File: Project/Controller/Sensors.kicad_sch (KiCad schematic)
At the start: 8 parts, among them J4 Conn_01x04, U3 BMI088, U4 MMC5983MA

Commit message: Add LDO to power input for controller board
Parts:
- renumbered C17 to C18, C18 to C19, C19 to C20, C20 to C21, C21 to C22, U3 to U5, U4 to U6
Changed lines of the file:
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@@
 		(dnp no)
 		(fields_autoplaced yes)
-		(property "Reference" "#PWR037"
+		(property "Reference" "#PWR040"
 			(at 147.32 107.95 0)
 			(effects
@@
 			(project "XuLabController"
 				(path "/71bb14ae-b730-4d22-a41d-cf68989dae2d/a5713b00-422c-456a-9938-13721b057665"
-					(reference "#PWR037")
+					(reference "#PWR040")
 					(unit 1)
 				)
@@
 		(dnp no)
 		(fields_autoplaced yes)
-		(property "Reference" "#PWR033"
+		(property "Reference" "#PWR036"
 			(at 215.9 76.2 0)
 			(effects
@@
 			(project "XuLabController"
 				(path "/71bb14ae-b730-4d22-a41d-cf68989dae2d/a5713b00-422c-456a-9938-13721b057665"
-					(reference "#PWR033")
+					(reference "#PWR036")
 					(unit 1)
 				)
@@
 		(dnp no)
 		(fields_autoplaced yes)
-		(property "Reference" "#PWR029"
+		(property "Reference" "#PWR032"
 			(at 139.7 63.5 0)
 			(effects
@@
 			(project "XuLabController"
 				(path "/71bb14ae-b730-4d22-a41d-cf68989dae2d/a5713b00-422c-456a-9938-13721b057665"
-					(reference "#PWR029")
+					(reference "#PWR032")
 					(unit 1)
 				)
@@
 		(dnp no)
 		(fields_autoplaced yes)
-		(property "Reference" "#PWR026"
+		(property "Reference" "#PWR029"
 			(at 127 48.26 0)
 			(effects
@@
 			(project "XuLabController"
 				(path "/71bb14ae-b730-4d22-a41d-cf68989dae2d/a5713b00-422c-456a-9938-13721b057665"
-					(reference "#PWR026")
+					(reference "#PWR029")
 					(unit 1)
 				)
@@
 		(dnp no)
 		(fields_autoplaced yes)
-		(property "Reference" "C20"
+		(property "Reference" "C21"
 			(at 151.13 109.2199 0)
 			(effects
@@
 			(project "XuLabController"
 				(path "/71bb14ae-b730-4d22-a41d-cf68989dae2d/a5713b00-422c-456a-9938-13721b057665"
-					(reference "C20")
+					(reference "C21")
 					(unit 1)
 				)
@@
 		(dnp no)
 		(fields_autoplaced yes)
-		(property "Reference" "#PWR035"
+		(property "Reference" "#PWR038"
 			(at 215.9 91.44 0)
 			(effects
@@
 			(project "XuLabController"
 				(path "/71bb14ae-b730-4d22-a41d-cf68989dae2d/a5713b00-422c-456a-9938-13721b057665"
-					(reference "#PWR035")
+					(reference "#PWR038")
 					(unit 1)
 				)
@@
 		(dnp no)
 		(fields_autoplaced yes)
-		(property "Reference" "#PWR036"
+		(property "Reference" "#PWR039"
 			(at 54.61 101.6 0)
 			(effects
@@
 			(project "XuLabController"
 				(path "/71bb14ae-b730-4d22-a41d-cf68989dae2d/a5713b00-422c-456a-9938-13721b057665"
-					(reference "#PWR036")
+					(reference "#PWR039")
 					(unit 1)
 				)
@@
 		(dnp no)
 		(fields_autoplaced yes)
-		(property "Reference" "U4"
+		(property "Reference" "U6"
 			(at 88.9 88.9 0)
 			(effects
@@
 			(project "XuLabController"
 				(path "/71bb14ae-b730-4d22-a41d-cf68989dae2d/a5713b00-422c-456a-9938-13721b057665"
-					(reference "U4")
+					(reference "U6")
 					(unit 1)
 				)
@@
 		(dnp no)
 		(fields_autoplaced yes)
-		(property "Reference" "#PWR027"
+		(property "Reference" "#PWR030"
 			(at 139.7 48.26 0)
 			(effects
@@
 			(project "XuLabController"
 				(path "/71bb14ae-b730-4d22-a41d-cf68989dae2d/a5713b00-422c-456a-9938-13721b057665"
-					(reference "#PWR027")
+					(reference "#PWR030")
 					(unit 1)
 				)
@@
 		(dnp no)
 		(fields_autoplaced yes)
-		(property "Reference" "#PWR040"
+		(property "Reference" "#PWR043"
 			(at 124.46 129.54 0)
 			(effects
@@
 			(project "XuLabController"
 				(path "/71bb14ae-b730-4d22-a41d-cf68989dae2d/a5713b00-422c-456a-9938-13721b057665"
-					(reference "#PWR040")
+					(reference "#PWR043")
 					(unit 1)
 				)
@@
 		(dnp no)
 		(fields_autoplaced yes)
-		(property "Reference" "C17"
+		(property "Reference" "C18"
 			(at 130.81 49.5299 0)
 			(effects
@@
 			(project "XuLabController"
 				(path "/71bb14ae-b730-4d22-a41d-cf68989dae2d/a5713b00-422c-456a-9938-13721b057665"
-					(reference "C17")
+					(reference "C18")
 					(unit 1)
 				)
@@
 		(on_board yes)
 		(dnp no)
-		(property "Reference" "#PWR034"
+		(property "Reference" "#PWR037"
 			(at 185.42 88.9 0)
 			(effects
@@
 			(project "XuLabController"
 				(path "/71bb14ae-b730-4d22-a41d-cf68989dae2d/a5713b00-422c-456a-9938-13721b057665"
-					(reference "#PWR034")
+					(reference "#PWR037")
 					(unit 1)
 				)
@@
 		(dnp no)
 		(fields_autoplaced yes)
-		(property "Reference" "#PWR032"
+		(property "Reference" "#PWR035"
 			(at 185.42 76.2 0)
 			(effects
@@
 			(project "XuLabController"
 				(path "/71bb14ae-b730-4d22-a41d-cf68989dae2d/a5713b00-422c-456a-9938-13721b057665"
-					(reference "#PWR032")
+					(reference "#PWR035")
 					(unit 1)
 				)
@@
 		(dnp no)
 		(fields_autoplaced yes)
-		(property "Reference" "C19"
+		(property "Reference" "C20"
 			(at 219.71 77.4699 0)
 			(effects
@@
 			(project "XuLabController"
 				(path "/71bb14ae-b730-4d22-a41d-cf68989dae2d/a5713b00-422c-456a-9938-13721b057665"
-					(reference "C19")
+					(reference "C20")
 					(unit 1)
 				)
@@
 		(dnp no)
 		(fields_autoplaced yes)
-		(property "Reference" "C21"
+		(property "Reference" "C22"
 			(at 133.35 116.8399 0)
 			(effects
@@
 			(project "XuLabController"
 				(path "/71bb14ae-b730-4d22-a41d-cf68989dae2d/a5713b00-422c-456a-9938-13721b057665"
-					(reference "C21")
+					(reference "C22")
 					(unit 1)
 				)
@@
 		(dnp no)
 		(fields_autoplaced yes)
-		(property "Reference" "#PWR031"
+		(property "Reference" "#PWR034"
 			(at 86.36 74.93 0)
 			(effects
@@
 			(project "XuLabController"
 				(path "/71bb14ae-b730-4d22-a41d-cf68989dae2d/a5713b00-422c-456a-9938-13721b057665"
-					(reference "#PWR031")
+					(reference "#PWR034")
 					(unit 1)
 				)
@@
 		(dnp no)
 		(fields_autoplaced yes)
-		(property "Reference" "U3"
+		(property "Reference" "U5"
 			(at 93.5833 33.02 0)
 			(effects
@@
 			(project "XuLabController"
 				(path "/71bb14ae-b730-4d22-a41d-cf68989dae2d/a5713b00-422c-456a-9938-13721b057665"
-					(reference "U3")
+					(reference "U5")
 					(unit 1)
 				)
@@
 		(dnp no)
 		(fields_autoplaced yes)
-		(property "Reference" "#PWR025"
+		(property "Reference" "#PWR028"
 			(at 86.36 35.56 0)
 			(effects
@@
 			(project "XuLabController"
 				(path "/71bb14ae-b730-4d22-a41d-cf68989dae2d/a5713b00-422c-456a-9938-13721b057665"
-					(reference "#PWR025")
+					(reference "#PWR028")
 					(unit 1)
 				)
@@
 		(dnp no)
 		(fields_autoplaced yes)
-		(property "Reference" "#PWR039"
+		(property "Reference" "#PWR042"
 			(at 147.32 123.19 0)
 			(effects
@@
 			(project "XuLabController"
 				(path "/71bb14ae-b730-4d22-a41d-cf68989dae2d/a5713b00-422c-456a-9938-13721b057665"
-					(reference "#PWR039")
+					(reference "#PWR042")
 					(unit 1)
 				)
@@
 		(dnp no)
 		(fields_autoplaced yes)
-		(property "Reference" "C18"
+		(property "Reference" "C19"
 			(at 143.51 49.5299 0)
 			(effects
@@
 			(project "XuLabController"
 				(path "/71bb14ae-b730-4d22-a41d-cf68989dae2d/a5713b00-422c-456a-9938-13721b057665"
-					(reference "C18")
+					(reference "C19")
 					(unit 1)
 				)
@@
 		(dnp no)
 		(fields_autoplaced yes)
-		(property "Reference" "#PWR028"
+		(property "Reference" "#PWR031"
 			(at 127 63.5 0)
 			(effects
@@
 			(project "XuLabController"
 				(path "/71bb14ae-b730-4d22-a41d-cf68989dae2d/a5713b00-422c-456a-9938-13721b057665"
-					(reference "#PWR028")
+					(reference "#PWR031")
 					(unit 1)
 				)
@@
 		(dnp no)
 		(fields_autoplaced yes)
-		(property "Reference" "#PWR030"
+		(property "Reference" "#PWR033"
 			(at 74.93 69.85 0)
 			(effects
@@
 			(project "XuLabController"
 				(path "/71bb14ae-b730-4d22-a41d-cf68989dae2d/a5713b00-422c-456a-9938-13721b057665"
-					(reference "#PWR030")
+					(reference "#PWR033")
 					(unit 1)
 				)
@@
 		(dnp no)
 		(fields_autoplaced yes)
-		(property "Reference" "#PWR038"
+		(property "Reference" "#PWR041"
 			(at 123.19 106.68 0)
 			(effects
@@
 			(project "XuLabController"
 				(path "/71bb14ae-b730-4d22-a41d-cf68989dae2d/a5713b00-422c-456a-9938-13721b057665"
-					(reference "#PWR038")
-					(unit 1)
-				)
+					(reference "#PWR041")
+					(unit 1)
+				)

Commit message: Relabel Bar30 I2C connector
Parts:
- J4: value Conn_01x04 -> Bar30
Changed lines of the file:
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@@
 			)
 		)
-		(property "Value" "Conn_01x04"
+		(property "Value" "Bar30"
 			(at 193.04 78.7399 0)
 			(effects

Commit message: Add ideal diode ORing for power connector and USB power
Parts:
- renumbered C18 to C20, C19 to C21, C20 to C22, C21 to C23, C22 to C24, U5 to U7, U6 to U8
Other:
- moved on the sheet: C22

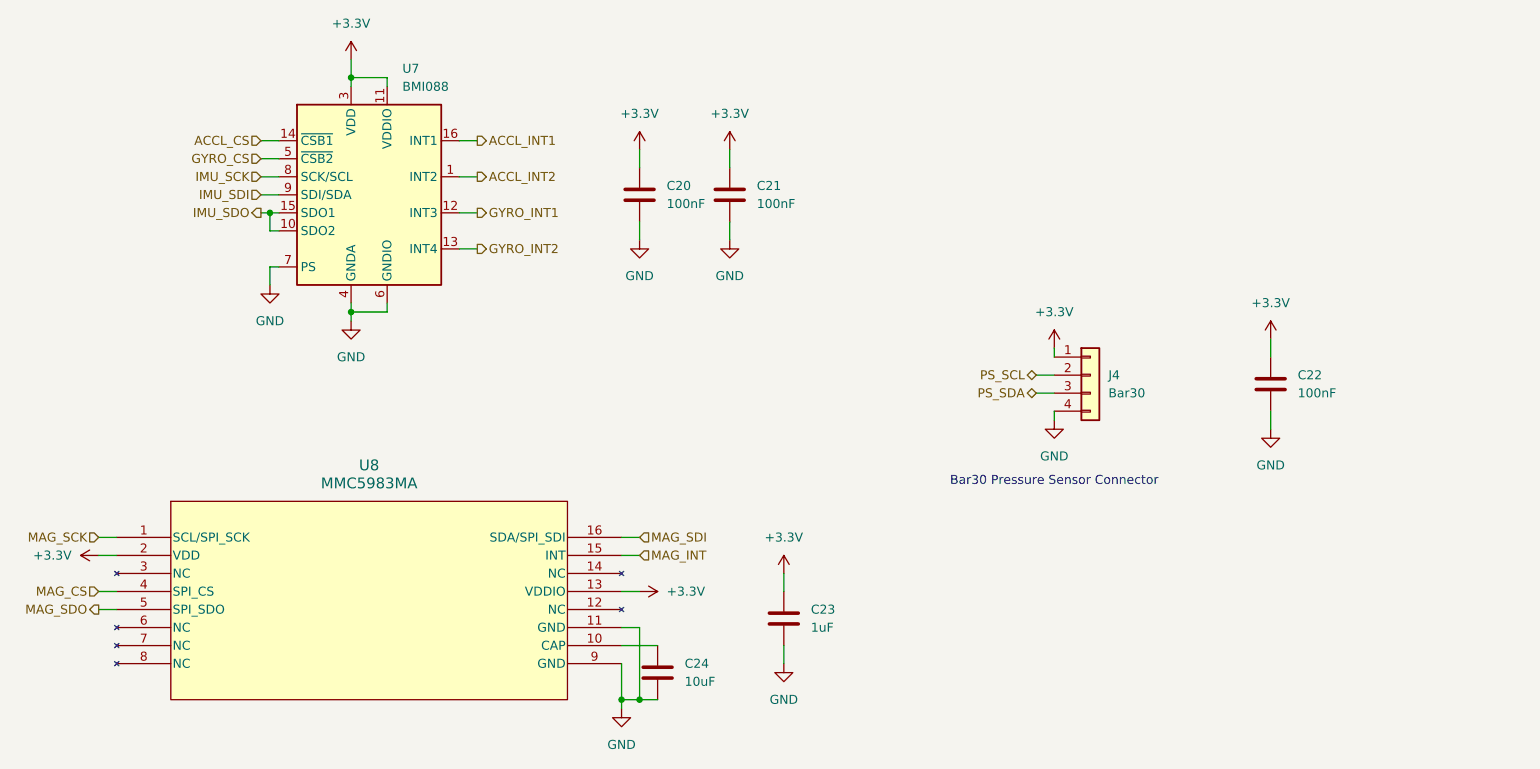
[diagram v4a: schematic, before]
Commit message: Add MCP9700A temperature sensor
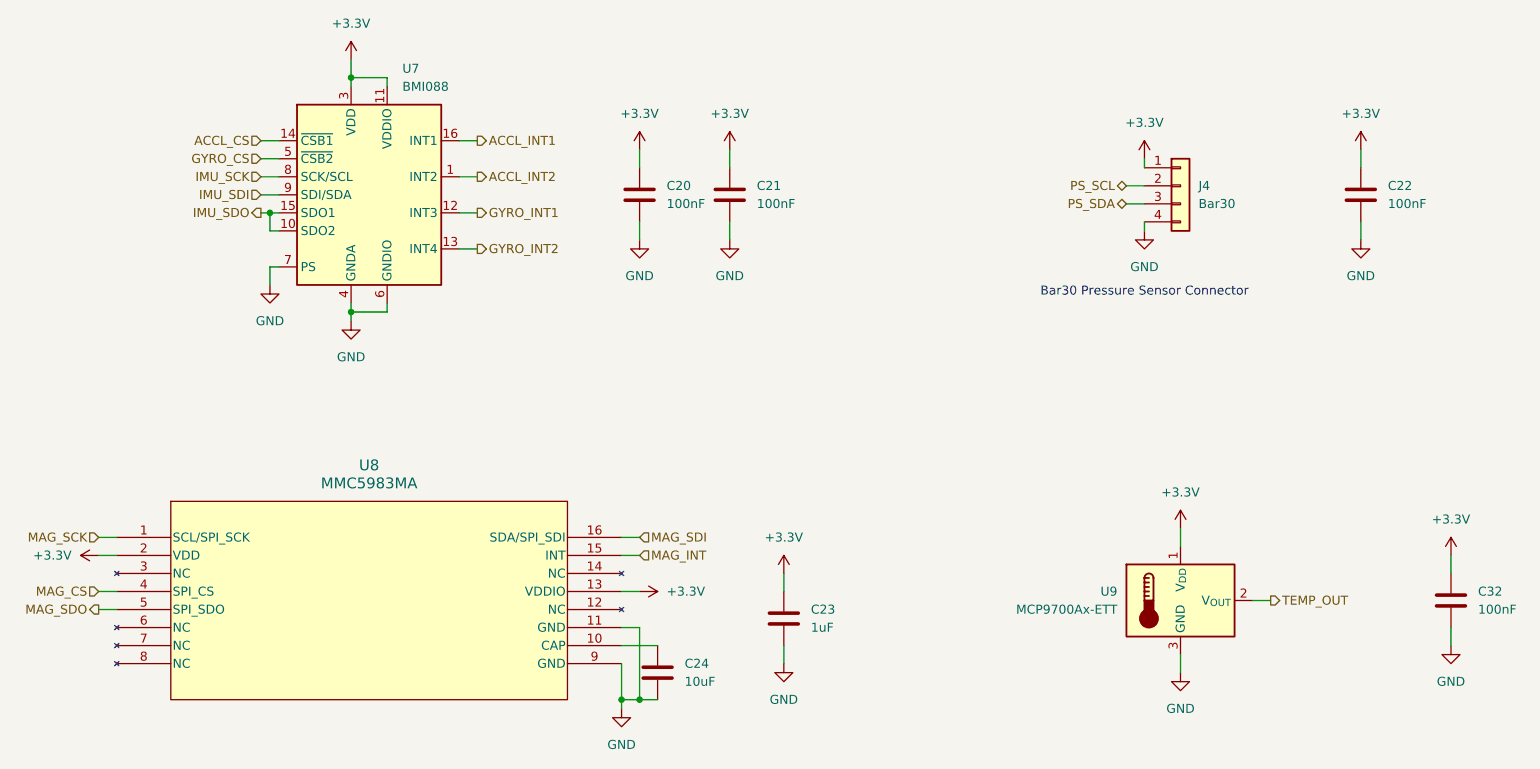
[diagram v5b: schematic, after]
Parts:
- added C32: 100nF, Capacitor_SMD:C_0402_1005Metric, symbol Device:C
- added U9: MCP9700Ax-ETT, Package_TO_SOT_SMD:SOT-23, symbol Sensor_Temperature:MCP9700Ax-ETT
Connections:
- net +3.3V: now also C32.1, U9.1 (V_{DD})
- net GND: now also C32.2, U9.3 (GND)
- new net TEMP_OUT: U9.2 (V_{OUT})
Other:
- moved on the sheet: C22, J4
